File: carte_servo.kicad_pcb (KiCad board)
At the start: 4 copper layers, 172.4 x 152.6 mm, 135 parts, among them J10 Conn_01x03_Male, J11 Transistor_2, J12 Transistor_1, J13 Transistor_4, J14 Transistor_.3, J16 Conn_01x04_Male, J17 Conn_01x04_Male, J18 Conn_01x03_Male, J19 Conn_01x03_Male, J2 Conn_02x04_Top_Bottom, J20 Stepper, J21 Stepper, J24 Conn_LEDs, J25 Conn_AX12, J29 Conn_AX12, J5 Conn_01x03_Male, J6 Conn_01x03_Male, J7 Conn_01x03_Male, J8 Conn_01x03_Male, J9 Conn_01x03_Male, P1 USB_C_Plug_USB2.0, Q1 DMN2011UTS, Q2 DMN2011UTS, Q3 DMN2011UTS, Q4 DMN2011UTS, Q6 DMN2011UTS, Q7 CSD17307Q5A, Q8 CSD17579Q5A, SW1 CK_KMS2xxG, U1 XGZP6897D_differential_pressu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, U10 TPS563200, U2 XGZP6897D_differential_pressu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, U3 TMC2208_SILENTSTEPSTICK, U4 TMC2208_SILENTSTEPSTICK, U5 74LVC2G241, U6 SN65HVD230, U7 LD1117S33TR_SOT223, U8 ESP32-S3-WROOM-1, U9 LM3150MH

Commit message: continue routing
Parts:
- moved C1 64.2 mm to (143.9, 126.2)
- moved U1 59.4 mm to (147.0, 118.5), turned to 90 degrees
- moved U2 26.1 mm to (206.8, 91.5)
- moved C2 19.7 mm to (216.2, 89.4)
- moved D37 9.74 mm to (142.8, 108.7), turned to -90 degrees
- moved J16 8.59 mm to (145.0, 102.2), turned to 0 degrees
- moved J17 8.59 mm to (148.8, 102.2), turned to 0 degrees
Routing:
- net SCL: track 24.3 -> 8.30 mm
- net 5V: track 100.4 -> 113.1 mm
- net GND: track 323.3 -> 330.2 mm
- net SDA: track 15.2 -> 11.7 mm
- net 12V_ELEC_P: track 0.00 -> 3.00 mm
- net BATT_12V: track 114.8 -> 112.2 mm
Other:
- board size 172.4 x 152.6 mm -> 52.6 x 102.8 mm

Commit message: continue routing
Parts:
- added C11: 4.7µF, Capacitor_SMD:C_0603_1608Metric, F.Cu at (179.2, 97.0)
- added C8: 100nF, Capacitor_SMD:C_0603_1608Metric, F.Cu at (159.2, 88.8)
- C11: value 100nF -> 4.7µF
- C4: moved to B.Cu
- D21, D22, D23, D24, D28, D30, D32, D33, D36, R4: moved to F.Cu
- moved C3 70.1 mm to (147.8, 77.6)
- moved C4 64.5 mm to (147.8, 98.0), turned to 180 degrees
- moved G*** 54.2 mm to (168.2, 83.8)
- moved D24 50.7 mm to (171.8, 72.8), turned to -90 degrees
- moved R37 50.3 mm to (128.2, 124.8)
- moved D23 48.5 mm to (175.6, 72.0), turned to 0 degrees
- moved R26 45.3 mm to (126.8, 120.4)
- moved C2 45.0 mm to (173.0, 77.0), turned to -90 degrees
- moved D30 42.0 mm to (162.2, 75.2), turned to 90 degrees
- moved D32 30.1 mm to (158.4, 77.0), turned to 180 degrees
- moved U2 28.7 mm to (180.6, 79.7), turned to 0 degrees
- moved D21 20.7 mm to (152.2, 73.0), turned to -90 degrees
- moved D22 19.7 mm to (143.6, 69.0), turned to 180 degrees
- moved D1 15.3 mm to (152.0, 99.0), turned to -90 degrees
- moved D38 11.8 mm to (143.0, 108.8), turned to -90 degrees
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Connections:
- C11 pad 1: Pressure_2 -> 3.3V
- U8 pad 12: STEP_1 -> STEP_2
- U8 pad 19: STEP_2 -> STEP_1
- U8 pad 28: SERVO_2 -> SERVO_1
- U8 pad 29: SERVO_7 -> SERVO_2
- U8 pad 32: SERVO_6 -> SERVO_4
- U8 pad 34: SERVO_1 -> SERVO_6
- U8 pad 35: SERVO_4 -> SERVO_7
- U8 pad 38: sense_5V -> Pressure_2
- U8 pad 5: Pressure_2 -> sense_5V
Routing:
- net GND: track 330.2 -> 493.9 mm, vias 0 -> 1
- net BATT_12V: track 112.2 -> 240.9 mm, vias 0 -> 3
- net DIR_1: track 0.00 -> 64.1 mm
- net STEP_1: track 0.00 -> 62.6 mm
- net SCL: track 8.30 -> 61.7 mm
- net SDA: track 11.7 -> 51.4 mm
- net 3.3V: track 22.4 -> 58.2 mm, vias 0 -> 2
- net SERVO_8: track 0.00 -> 35.8 mm
- net SERVO_7: track 0.00 -> 35.3 mm
- net SERVO_2: track 0.00 -> 33.3 mm
- net Pressure_2: track 0.00 -> 31.1 mm, vias 0 -> 2
- net SERVO_3: track 0.00 -> 27.3 mm
- net SERVO_4: track 0.00 -> 26.4 mm
- net SERVO_6: track 2.90 -> 27.1 mm
- net SERVO_5: track 4.31 -> 26.0 mm
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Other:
- board size 52.6 x 102.8 mm -> 52.4 x 99.2 mm

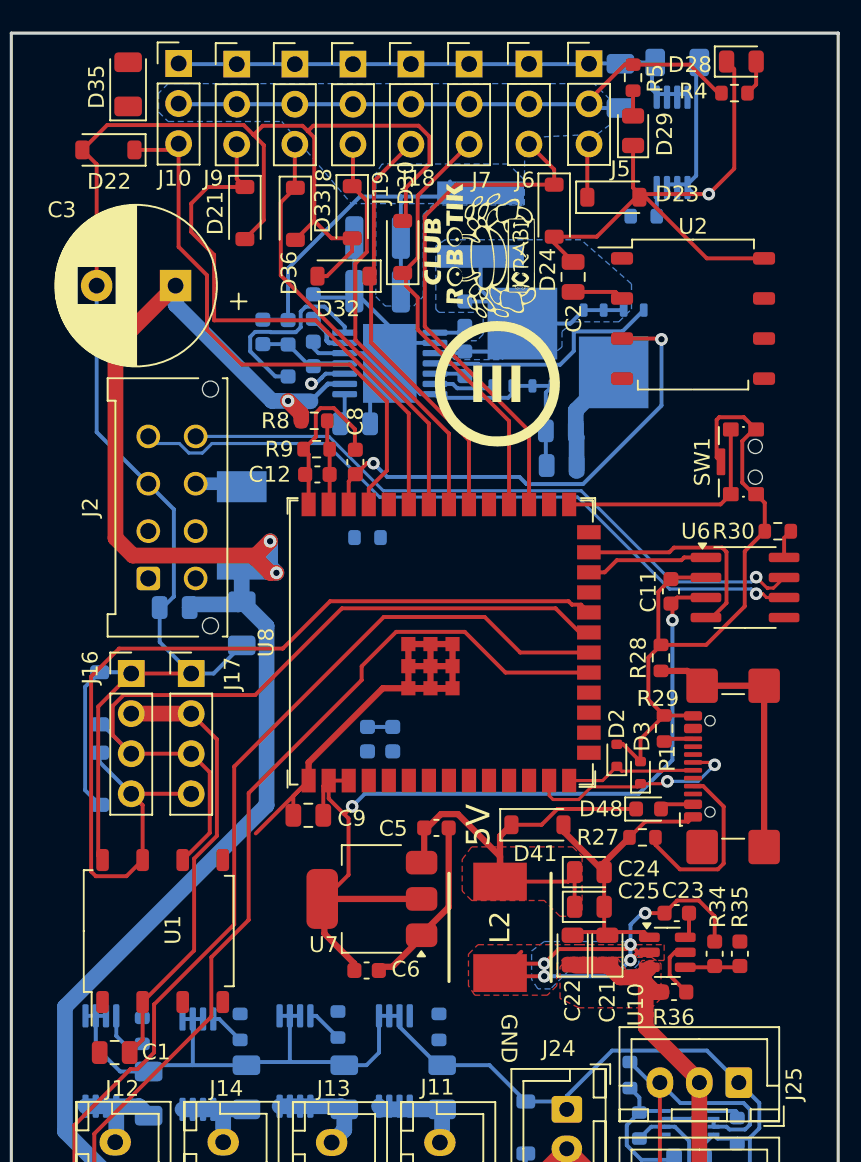
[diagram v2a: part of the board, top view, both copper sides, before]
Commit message: continue routing. Shorter SW_6V and 12V from connector to big capa
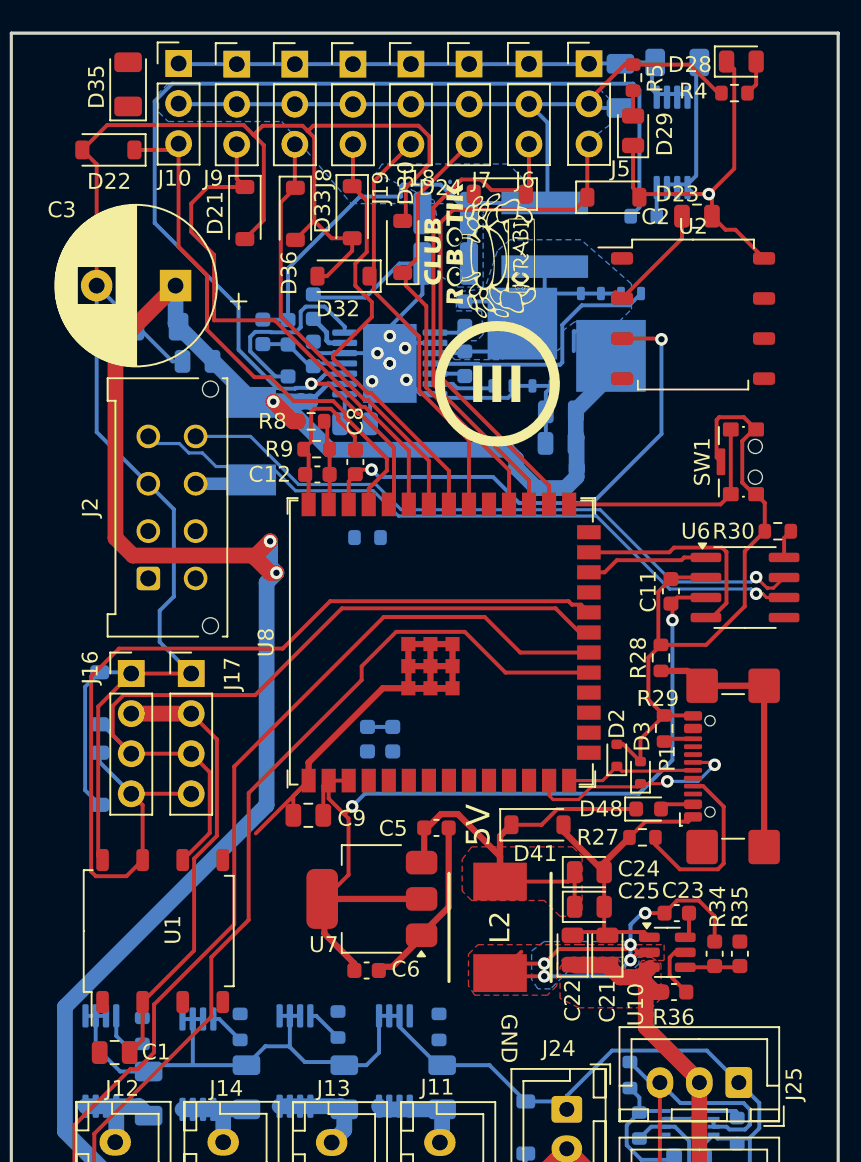
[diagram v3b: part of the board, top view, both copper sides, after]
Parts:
- moved D1 19.6 mm to (146.6, 80.2), turned to 180 degrees
- moved C4 15.7 mm to (149.2, 82.4)
- moved C2 8.74 mm to (180.8, 73.2), turned to 180 degrees
- moved F1 5.38 mm to (152.6, 87.5), turned to -90 degrees
- moved C16 4.66 mm to (164.9, 76.2)
- moved C17 4.58 mm to (164.9, 73.0)
- moved L1 4.11 mm to (171.2, 74.4)
- moved D24 3.61 mm to (168.3, 71.8), turned to 180 degrees
- moved C20 1.40 mm to (172.2, 87.6)
- moved C19 1.20 mm to (172.2, 85.6)
- moved Q7 1.06 mm to (175.4, 81.0)
- moved R8 0.20 mm to (156.4, 86.2)
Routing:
- net ENABLE_SERVO_POWER_1: track 2.38 -> 76.3 mm
- net SERVO_1: track 3.23 -> 33.9 mm
- net BATT_12V: track 240.9 -> 266.7 mm
- net /ServoDCDC/VOUT: track 63.6 -> 73.7 mm
- net GND: track 493.9 -> 485.9 mm, vias 1 -> 8
- net 5V: track 116.4 -> 120.5 mm
- net SERVO_5: track 26.0 -> 28.1 mm
- net SERVO_2: track 33.3 -> 31.2 mm
- net SERVO_8: track 35.8 -> 33.8 mm
- net Pressure_2: track 31.1 -> 32.8 mm
- net SERVO_7: track 35.3 -> 33.9 mm
- net Net-(Q7-G): track 15.4 -> 16.4 mm

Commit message: basic routing
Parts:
- removed the C11 at (161.6, 106.3)
- R23: moved to F.Cu
- R26, R37: moved to B.Cu
- moved R3 85.2 mm to (153.8, 120.6), turned to -90 degrees
- moved D27 80.0 mm to (153.8, 117.3), turned to -90 degrees
- moved R25 50.1 mm to (165.2, 143.4), turned to 90 degrees
- moved G*** 45.2 mm to (159.2, 96.6)
- moved R12 41.5 mm to (171.4, 97.8), turned to -90 degrees
- moved R37 38.6 mm to (163.6, 140.2)
- moved R26 38.3 mm to (158.6, 141.8), turned to 180 degrees
- moved R23 33.8 mm to (176.2, 98.2), turned to 90 degrees
- moved U5 9.49 mm to (172.4, 125.4)
- moved C7 9.37 mm to (172.6, 127.8)
- moved R22 8.97 mm to (169.2, 126.8), turned to 90 degrees
- moved R17 8.05 mm to (157.0, 121.6), turned to 0 degrees
- moved R34 4.78 mm to (179.6, 115.8), turned to 0 degrees
- moved D24 4.10 mm to (164.2, 71.8)
- moved G*** 1.81 mm to (168.8, 75.6)
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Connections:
- U2 pad 6: SDA -> unconnected-(U2-SDA-Pad6)
- U2 pad 7: SCL -> unconnected-(U2-SCL-Pad7)
- U8 pad 18: DIR_2 -> LEDs
- U8 pad 6: LEDs -> DIR_2
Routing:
- net 5V: track 120.5 -> 275.0 mm, vias 0 -> 4
- net GND: track 485.9 -> 606.9 mm, vias 8 -> 13
- net ENABLE_STEPPER_POWER: track 25.6 -> 80.2 mm, vias 0 -> 2
- net AX12_tx_en: track 4.85 -> 56.7 mm, vias 0 -> 1
- net sense_5V: track 0.00 -> 49.9 mm, vias 0 -> 1
- net BATT_12V: track 266.7 -> 312.4 mm
- net STEP_2: track 0.00 -> 45.0 mm, vias 0 -> 1
- net LEDs: track 1.96 -> 44.9 mm, vias 0 -> 1
- net DIR_2: track 0.00 -> 37.4 mm, vias 0 -> 1
- net TRANSISTOR_1: track 0.00 -> 28.0 mm, vias 0 -> 1
- net TRANSISTOR_2: track 0.00 -> 27.8 mm, vias 0 -> 1
- net Pressure_1: track 0.00 -> 26.1 mm, vias 0 -> 2
- net AX12_master_TX: track 0.00 -> 25.9 mm, vias 0 -> 1
- net TRANSISTOR_3: track 0.00 -> 25.1 mm, vias 0 -> 1
- net TRANSISTOR_4: track 0.00 -> 22.4 mm, vias 0 -> 1
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- added copper zone on B.Cu, net GND
- added copper zone on F.Cu, net GND
- added copper zone on In1.Cu, net GND
- added copper zone on In2.Cu, net GND
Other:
- board size 52.4 x 99.2 mm -> 48.4 x 99.2 mm
- board text added: "Carte Actionneurs Victor Dubois Coupe 2024/2026"
- board text removed: "Carte Servo/Vide Victor Dubois Coupe 2023/2024"
- board text removed: "Carte Servo/Vide Victor Dubois Coupe 2023/4"
- board text removed: "servo power"

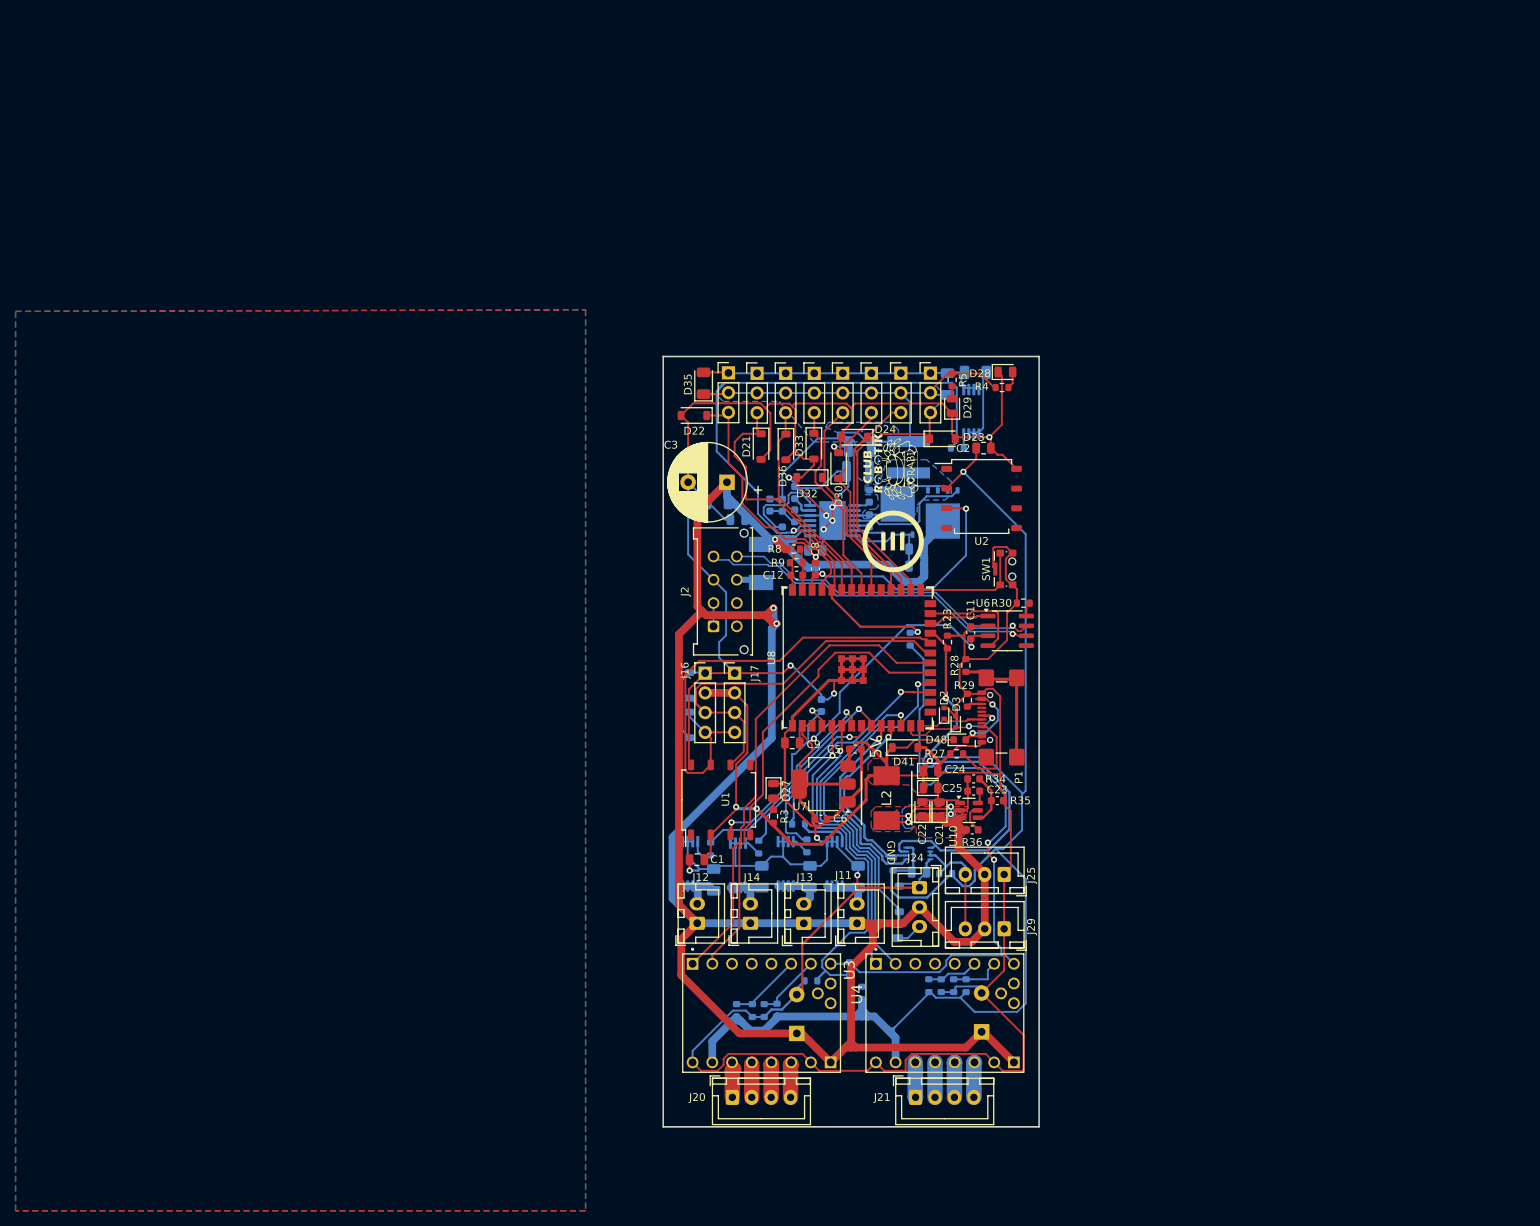
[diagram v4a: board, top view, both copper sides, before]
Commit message: widen 12V/5V
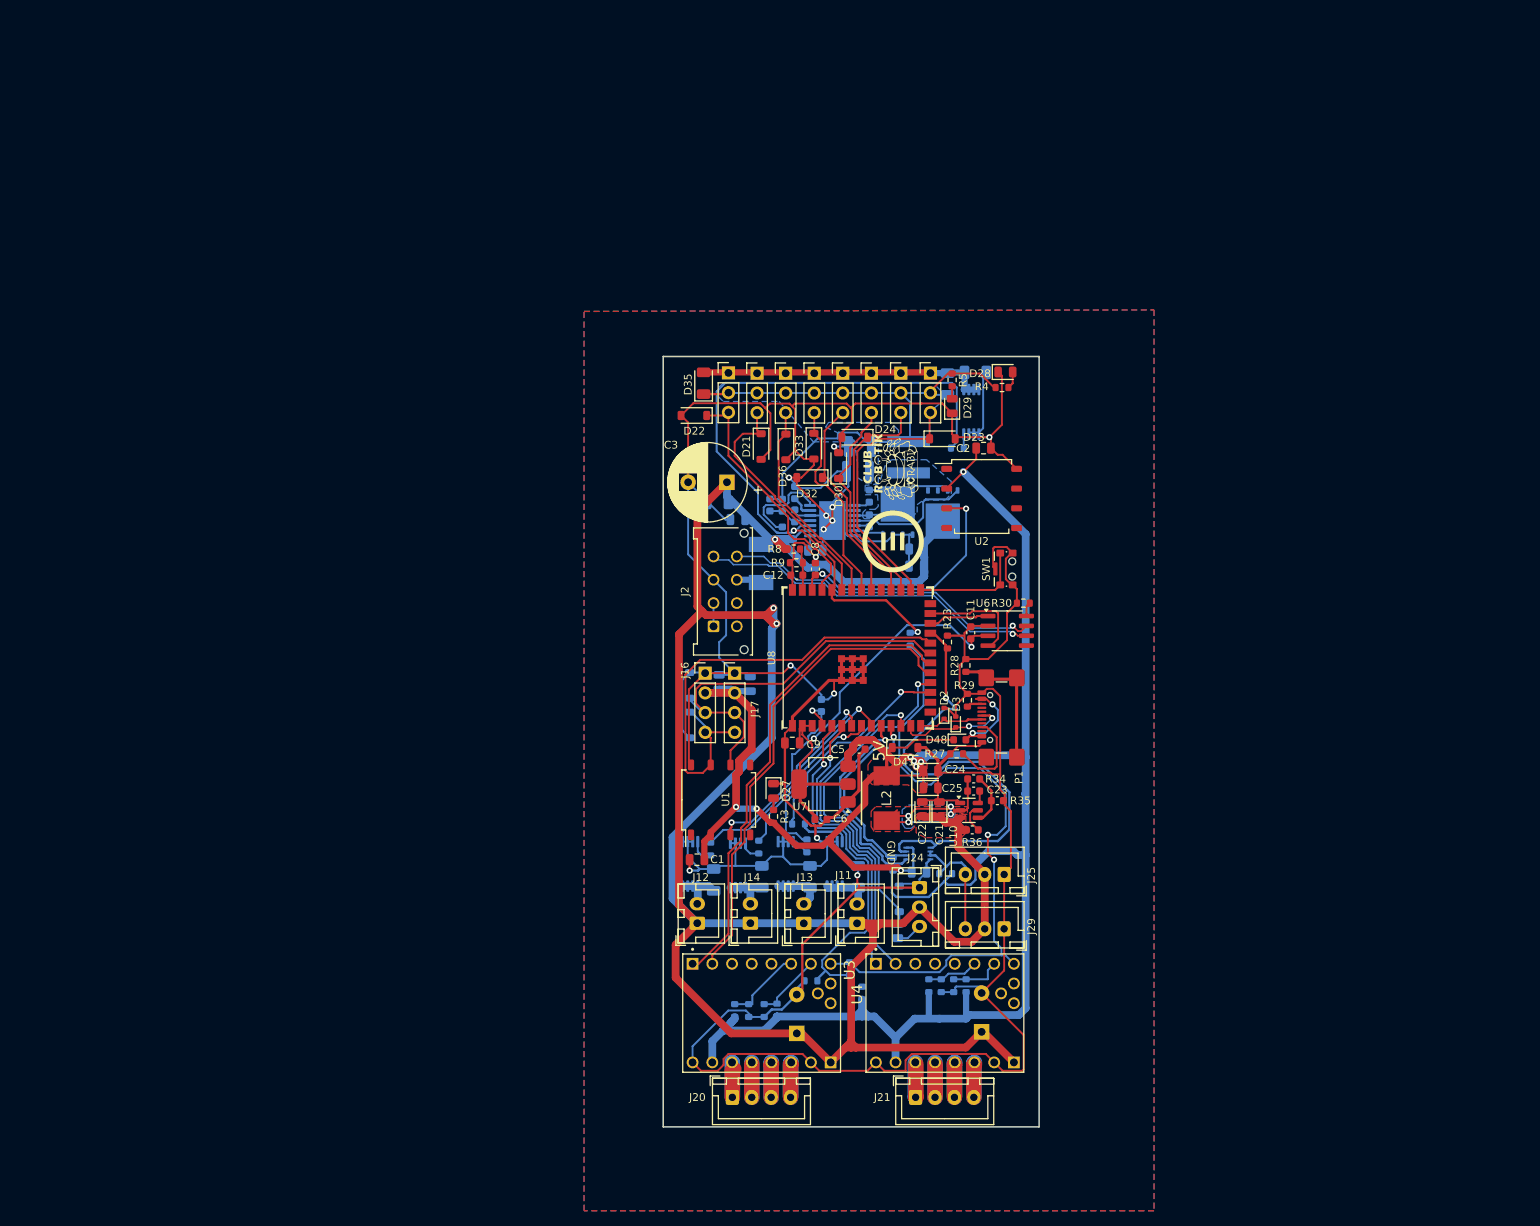
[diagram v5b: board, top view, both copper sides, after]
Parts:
- added C28: 100nF, Capacitor_SMD:C_0805_2012Metric, B.Cu at (150.8, 103.5)
- added C29: 100nF, Capacitor_SMD:C_0805_2012Metric, B.Cu at (146.8, 103.3)
- moved C5 0.48 mm to (164.8, 112.0)
- moved R11 0.48 mm to (150.6, 145.6)
- moved R7 0.24 mm to (148.8, 145.6)
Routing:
- net 5V: track 275.0 -> 341.1 mm, vias 4 -> 8
- net GND: track 606.9 -> 613.7 mm
- net AX12_tx_en: track 56.7 -> 61.4 mm
- net /stepper_driver/OA2: track 4.41 -> 8.94 mm
- net /stepper_driver/OA1: track 4.34 -> 8.85 mm
- net /stepper_driver/OB2: track 3.76 -> 8.28 mm
- net /stepper_driver/OB1: track 4.26 -> 8.76 mm
- net /stepper_driver1/OA2: track 4.53 -> 8.83 mm
- net /stepper_driver1/OA1: track 4.52 -> 8.80 mm
- net /stepper_driver1/OB1: track 4.50 -> 8.76 mm
- net /stepper_driver1/OB2: track 4.52 -> 8.77 mm
- net ENABLE_STEPPER_POWER: track 80.2 -> 83.5 mm
- net SERVO_7: track 33.9 -> 31.7 mm
- net STEP_1: track 60.0 -> 61.6 mm
- net SERVO_2: track 28.6 -> 30.1 mm
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
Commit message: add vias and stuff
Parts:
- moved SW1 2.63 mm to (186.4, 88.4)
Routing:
- net 5V: track 341.1 -> 308.9 mm
- net GND: track 613.7 -> 617.9 mm, vias 13 -> 90
- net BOOT: track 14.6 -> 17.6 mm
- net STEP_2: track 45.0 -> 42.1 mm
- net sense_5V: track 49.9 -> 47.1 mm
- net DIR_2: track 37.4 -> 34.6 mm
- net LEDs: track 44.9 -> 42.3 mm
- net /ServoDCDC/VOUT: track 76.9 -> 79.4 mm
- net ENABLE_SERVO_POWER_1: track 91.4 -> 93.8 mm
- net /DCDC_5V/SW_DCDC5V: track 28.0 -> 26.1 mm
- net AX12_tx_en: track 61.4 -> 60.2 mm
- net SERVO_1: track 33.9 -> 35.0 mm
- net SERVO_2: track 30.1 -> 30.9 mm
- net ENABLE_STEPPER_POWER: track 83.5 -> 82.8 mm
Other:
- board text added: "Carte Actionneurs Victor Dubois Coupe 2024/2025"
- board text removed: "Carte Actionneurs Victor Dubois Coupe 2024/2026"
